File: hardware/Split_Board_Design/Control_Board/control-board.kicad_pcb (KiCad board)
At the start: 2 copper layers, 100 x 60 mm, 118 parts, among them J1 USB2.0_16P, J10 Conn_01x03, J2 UART_CONN, J3 XT30PW-M, J5 Conn_01x06, J7 Conn_01x03, J8 Conn_01x03, J9 Conn_01x02, Q2 2SD882, Q3 BC817, Q4 BC817, Q5 2SD882, Q6 2SD882, SW1 ENABLE, U1 TCAN3414DR, U10 LTV-356T, U11 LTV-356T, U12 LTV-356T, U14 LTV-356T, U15 CH340C, U2 INA240A1PW, U3 MAX3485, U4 ESP32-WROOM-32E, U5 USBLC6-2SC6, U6 LTV-356T, U7 TLV1117-33, U8 LV14340DDAR

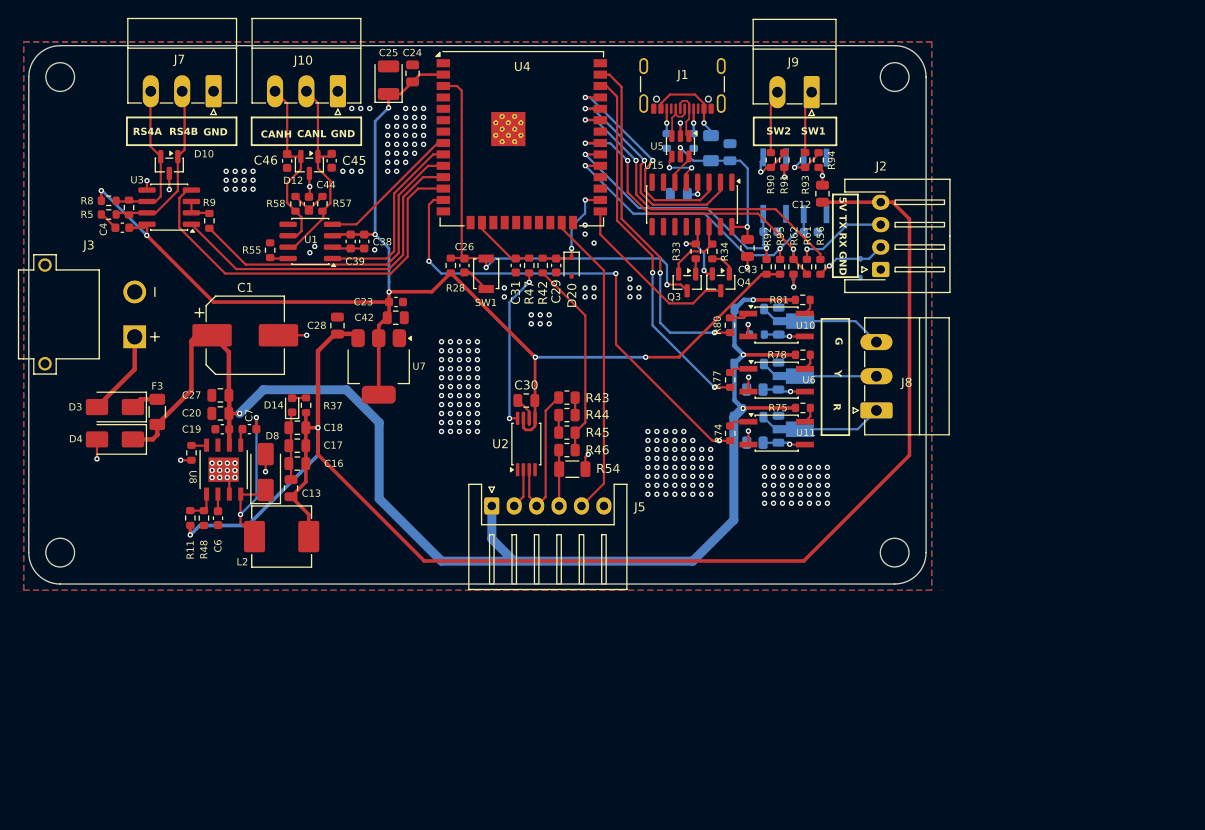
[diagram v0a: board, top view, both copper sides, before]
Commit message: feat(layout): Finished demo schematic for control board
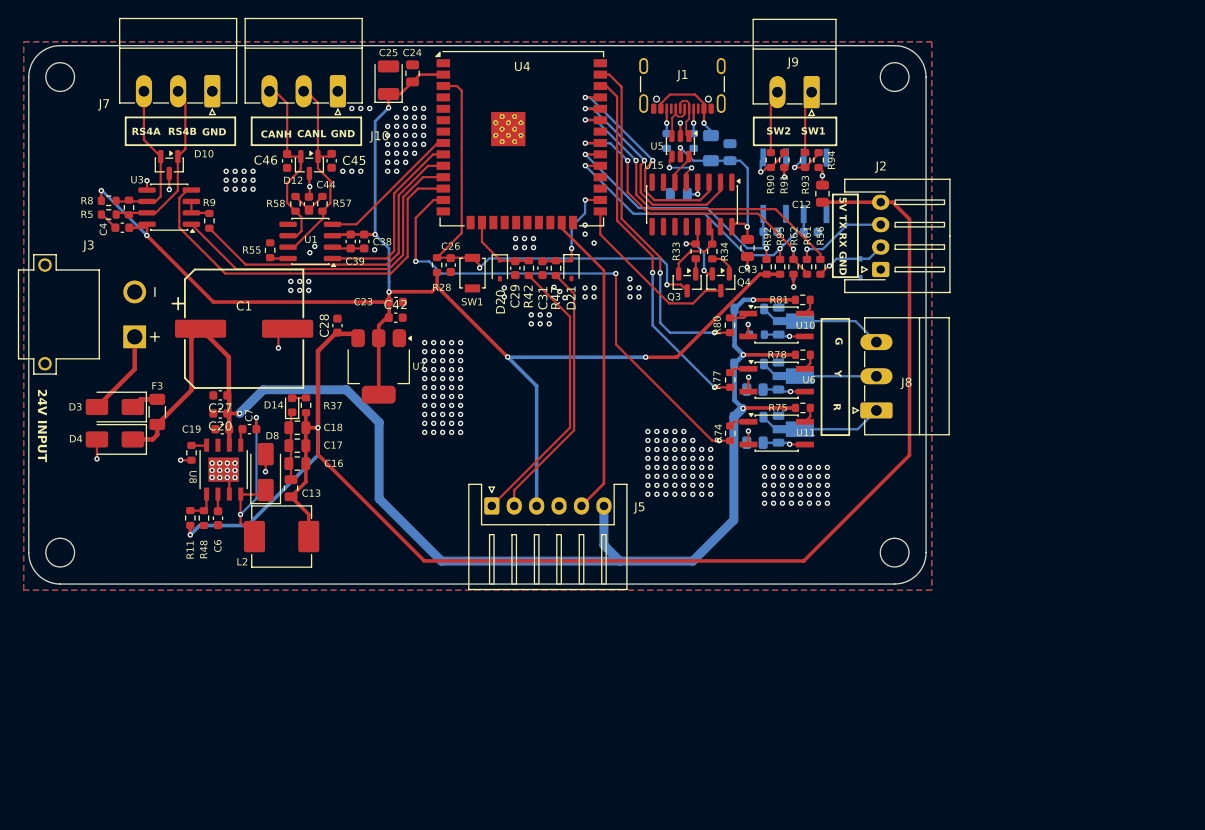
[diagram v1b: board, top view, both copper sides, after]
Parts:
- removed C30: 100nF, Capacitor_SMD:C_0805_2012Metric
- removed R43, R44, R45: 150kR, Resistor_SMD:R_0805_2012Metric
- removed R46: 18kR, Resistor_SMD:R_0805_2012Metric
- removed R54: 0R, Resistor_SMD:R_1206_3216Metric
- removed U2: INA240A1PW, Package_SO:TSSOP-8_4.4x3mm_P0.65mm
- added D21: PESD5Z3.3, Diode_SMD:D_SOD-323, F.Cu at (138.5, 62.9)
- C1: value 100uF -> 680uF-35V; footprint Capacitor_SMD:CP_Elec_8x10.5 -> RobotChargeController:CP_Elec_12.5x13.5_Generic_H13
- C20, C27, C28, C42: footprint Capacitor_SMD:C_0805_2012Metric -> Capacitor_SMD:C_0603_1608Metric
- C40, C41: value 100nF - 50V -> 100nF-50V
- J10, J7: footprint Connector_Phoenix_MC:PhoenixContact_MC_1,5_3-G-3.5_1x03_P3.50mm_Horizontal -> Connector_Phoenix_MC:PhoenixContact_MC_1,5_3-G-3.81_1x03_P3.81mm_Horizontal
- moved D20 8.01 mm to (130.5, 62.9)
- moved C29 4.56 mm to (132.2, 62.8)
- moved C31 2.99 mm to (135.2, 62.8)
- moved R47 2.99 mm to (136.8, 62.8)
- moved R42 1.58 mm to (133.7, 62.8)
- moved SW1 1.53 mm to (127.5, 63.4)
- moved R28 1.53 mm to (123.5, 62.5)
- moved C26 1.53 mm to (125.0, 62.5)
- moved C1 0.74 mm to (102.0, 69.5)
- moved J7 0.14 mm to (98.5, 43.1)
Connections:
- C29 pad 2: /MCU_Control/VOUT_SENSE_ADC -> /MCU_Control/VOUT_MCU_ADC
- C31 pad 2: /MCU_Control/IOUT_SENSE_ADC -> /MCU_Control/IOUT_MCU_ADC
- D20 pad 1: /MCU_Control/VOUT_SENSE_ADC -> /MCU_Control/VOUT_MCU_ADC
- J5 pad 1: +24V -> /MCU_Control/VOUT_SENSE_ADC
- J5 pad 2: /Output_Sensing/SHUNT_HIGH_P -> /MCU_Control/IOUT_SENSE_ADC
- J5 pad 3: /Output_Sensing/SHUNT_LOW_P -> +3V3
- J5 pad 4: 60V_GND -> GND
- J5 pad 6: GND -> +24V
- R42 pad 1: /MCU_Control/VOUT_SENSE_ADC -> /MCU_Control/VOUT_MCU_ADC
- R42 pad 2: Net-(R42-Pad2) -> /MCU_Control/VOUT_SENSE_ADC
- R47 pad 1: /MCU_Control/IOUT_SENSE_ADC -> /MCU_Control/IOUT_MCU_ADC
- R47 pad 2: Net-(R47-Pad2) -> /MCU_Control/IOUT_SENSE_ADC
- U4 pad 16: /MCU_Control/IOUT_SENSE_ADC -> /MCU_Control/VOUT_MCU_ADC
- U4 pad 26: /MCU_Control/VOUT_SENSE_ADC -> /MCU_Control/IOUT_MCU_ADC
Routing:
- net Net-(R42-Pad2): track 22.2 -> 0.00 mm
- net /MCU_Control/IOUT_SENSE_ADC: track 7.44 -> 29.3 mm
- net /MCU_Control/VOUT_SENSE_ADC: track 11.8 -> 31.2 mm, vias 2 -> 0
- net Net-(R47-Pad2): track 18.0 -> 0.00 mm, vias 2 -> 0
- net /Output_Sensing/SHUNT_LOW_P: track 17.5 -> 0.00 mm
- net /MCU_Control/IOUT_MCU_ADC: track 0.00 -> 12.1 mm, vias 0 -> 2
- net GND: track 49.4 -> 39.4 mm, vias 254 -> 268
- net +3V3: track 151.4 -> 159.7 mm
- net /MCU_Control/VOUT_MCU_ADC: track 0.00 -> 8.26 mm
- net 60V_GND: track 6.24 -> 0.00 mm
- net /Output_Sensing/SHUNT_HIGH_P: track 4.46 -> 0.00 mm
- net /MCU_Control/MCU_EN: track 51.6 -> 53.8 mm
- net /Communication_Interfaces/DO1_CMD: track 54.6 -> 56.7 mm
- net Net-(R44-Pad2): track 1.95 -> 0.00 mm
- net Net-(R43-Pad2): track 1.95 -> 0.00 mm
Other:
- board text added: "24V INPUT"

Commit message: feat(layout): Update layout
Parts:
- C12, C15, C18, C24, C43: value 100nF -> 100nF-50V; footprint Capacitor_SMD:C_0805_2012Metric -> Capacitor_SMD:C_0603_1608Metric
- C13: value 33pF -> 33pF-50V; footprint Capacitor_SMD:C_0805_2012Metric -> Capacitor_SMD:C_0603_1608Metric
- C16, C17: value 22uF -> 22uF-50V
- C21: value 10uF -> 10uF-50V; footprint Capacitor_SMD:C_0805_2012Metric -> Capacitor_SMD:C_0603_1608Metric
- C25: value 10uF -> 10uF-25V
- C6: value 22nF -> 22nF-50V
- moved F3 1.24 mm to (92.4, 80.0)
- moved C27 0.40 mm to (99.3, 77.4)
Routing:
- net +3V3: track 159.7 -> 158.8 mm
- net +24V: track 154.1 -> 154.9 mm
- net /Communication_Interfaces/DO1_CMD: vias 3 -> 2
- net GND: vias 268 -> 280
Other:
- board text added: "24V CTR GND 3V3 Vo Io"

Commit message: Some minor updates
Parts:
- C31: value 10nF-50V -> 100nF-50V
- R42: value 10kR -> 1kR
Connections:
- U4 pad 16: /MCU_Control/VOUT_MCU_ADC -> unconnected-(U4-IO13-Pad16)
- U4 pad 26: /MCU_Control/IOUT_MCU_ADC -> unconnected-(U4-IO4-Pad26)
- U4 pad 6: unconnected-(U4-IO34-Pad6) -> /MCU_Control/IOUT_MCU_ADC
- U4 pad 7: unconnected-(U4-IO35-Pad7) -> /MCU_Control/VOUT_MCU_ADC
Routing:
- net /MCU_Control/IOUT_MCU_ADC: track 12.1 -> 25.6 mm
- net /MCU_Control/VOUT_MCU_ADC: track 8.26 -> 21.0 mm, vias 0 -> 2
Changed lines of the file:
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@@
 			)
 		)
-		(property "Value" "10nF-50V"
+		(property "Value" "100nF-50V"
 			(at 0 1.43 90)
 			(layer "F.Fab")
@@
 			)
 		)
-		(property "Link to Buy" "https://linhkien.cxtvn.com/2353-tu-103-10nf-0603-50v-10-20c.html"
+		(property "Link to Buy" "https://linhkien.cxtvn.com/1981-tu-0603-khong-phan-cuc.html"
 			(at 0 0 90)
 			(unlocked yes)
@@
 			)
 		)
-		(property "Value" "10kR"
+		(property "Value" "1kR"
 			(at 0 1.43 90)
 			(layer "F.Fab")
@@
 			(size 1.5 0.9)
 			(layers "F.Cu" "F.Mask" "F.Paste")
-			(net "unconnected-(U4-IO34-Pad6)")
+			(net "/MCU_Control/IOUT_MCU_ADC")
 			(pinfunction "IO34_6")
-			(pintype "input+no_connect")
+			(pintype "input")
 		)
 		(pad "7" smd rect
@@
 			(size 1.5 0.9)
 			(layers "F.Cu" "F.Mask" "F.Paste")
-			(net "unconnected-(U4-IO35-Pad7)")
+			(net "/MCU_Control/VOUT_MCU_ADC")
 			(pinfunction "IO35_7")
-			(pintype "input+no_connect")
+			(pintype "input")
 		)
 		(pad "8" smd rect
@@
 			(size 1.5 0.9)
 			(layers "F.Cu" "F.Mask" "F.Paste")
-			(net "/MCU_Control/VOUT_MCU_ADC")
+			(net "unconnected-(U4-IO13-Pad16)")
 			(pinfunction "IO13_16")
-			(pintype "bidirectional")
+			(pintype "bidirectional+no_connect")
 		)
 		(pad "17" smd rect
@@
 			(size 1.5 0.9)
 			(layers "F.Cu" "F.Mask" "F.Paste")
-			(net "/MCU_Control/IOUT_MCU_ADC")
+			(net "unconnected-(U4-IO4-Pad26)")
 			(pinfunction "IO4_26")
-			(pintype "bidirectional")
+			(pintype "bidirectional+no_connect")
 		)
 		(pad "27" smd rect
@@
 	)
 	(segment
-		(start 126.25 43.025)
-		(end 125.725 42.5)
+		(start 123.505 61.625)
+		(end 126.35 58.78)
 		(width 0.25)
 		(layer "F.Cu")
@@
 	)
 	(segment
-		(start 125.725 42.5)
-		(end 124.2 42.5)
+		(start 126.35 58.78)
+		(end 126.35 43.125)
 		(width 0.25)
 		(layer "F.Cu")
@@
 	)
 	(segment
-		(start 123.505 61.625)
-		(end 126.25 58.88)
+		(start 127.45 61.65)
+		(end 128.25 62.45)
 		(width 0.25)
 		(layer "F.Cu")
@@
 	)
 	(segment
-		(start 127.45 61.65)
-		(end 128.25 62.45)
+		(start 125.725 42.5)
+		(end 124.2 42.5)
 		(width 0.25)
 		(layer "F.Cu")
@@
 	)
 	(segment
-		(start 126.25 58.88)
-		(end 126.25 43.025)
+		(start 126.35 43.125)
+		(end 125.725 42.5)
 		(width 0.25)
 		(layer "F.Cu")
@@
 	)
 	(segment
+		(start 125.535 46.31)
+		(end 125.55 46.325)
+		(width 0.25)
+		(layer "F.Cu")
+		(net "/MCU_Control/IOUT_MCU_ADC")
+	)
+	(segment
 		(start 138.5 60.6)
 		(end 138.5 61.825)
@@
 	)
 	(segment
-		(start 141.7 55.2)
-		(end 140.225 55.2)
+		(start 124.2 46.31)
+		(end 125.535 46.31)
 		(width 0.25)
 		(layer "F.Cu")
@@
 	)
 	(via
-		(at 140.025 55.2)
+		(at 138.5 60.6)
 		(size 0.6)
 		(drill 0.3)
@@
 	)
 	(via
-		(at 138.5 60.6)
+		(at 125.55 46.325)
 		(size 0.6)
 		(drill 0.3)
@@
 	)
 	(segment
-		(start 140 56.675)
-		(end 140 55.225)
+		(start 138.5 60.6)
+		(end 138.5 59.275)
 		(width 0.25)
 		(layer "B.Cu")
@@
 	)
 	(segment
-		(start 140 55.225)
-		(end 140.025 55.2)
+		(start 138.5 59.275)
+		(end 125.55 46.325)
 		(width 0.25)
 		(layer "B.Cu")
@@
 	)
 	(segment
-		(start 138.5 60.6)
-		(end 138.5 58.175)
+		(start 124.2 47.58)
+		(end 125.58 47.58)
 		(width 0.25)
-		(layer "B.Cu")
-		(net "/MCU_Control/IOUT_MCU_ADC")
+		(layer "F.Cu")
+		(net "/MCU_Control/VOUT_MCU_ADC")
 	)
 	(segment
-		(start 138.5 58.175)
-		(end 140 56.675)
+		(start 125.58 47.58)
+		(end 125.6 47.6)
 		(width 0.25)
-		(layer "B.Cu")
-		(net "/MCU_Control/IOUT_MCU_ADC")
+		(layer "F.Cu")
+		(net "/MCU_Control/VOUT_MCU_ADC")
 	)
 	(segment
-		(start 130.5 61.875)
-		(end 128.505 59.88)
+		(start 130.5 60.8)
+		(end 130.5 61.875)
 		(width 0.25)
 		(layer "F.Cu")
@@
 	)
 	(segment
-		(start 128.505 59.88)
-		(end 128.505 57.72)
+		(start 130.625 61.97)
+		(end 130.5 61.845)
 		(width 0.25)
 		(layer "F.Cu")
@@
 	)
 	(segment
-		(start 130.625 61.97)
-		(end 130.5 61.845)
+		(start 130.525 60.775)
+		(end 130.5 60.8)
 		(width 0.25)
 		(layer "F.Cu")
@@
 		(net "/MCU_Control/VOUT_MCU_ADC")
 	)
+	(via
+		(at 125.6 47.6)
+		(size 0.6)
+		(drill 0.3)
+		(layers "F.Cu" "B.Cu")
+		(net "/MCU_Control/VOUT_MCU_ADC")
+	)
+	(via
+		(at 130.525 60.775)
+		(size 0.6)
+		(drill 0.3)
+		(layers "F.Cu" "B.Cu")
+		(net "/MCU_Control/VOUT_MCU_ADC")
+	)
+	(segment
+		(start 128.505 50.505)
+		(end 125.6 47.6)
+		(width 0.25)
+		(layer "B.Cu")
+		(net "/MCU_Control/VOUT_MCU_ADC")
+	)
+	(segment
+		(start 130.525 60.775)
+		(end 128.505 58.755)
+		(width 0.25)
+		(layer "B.Cu")
+		(net "/MCU_Control/VOUT_MCU_ADC")
+	)
+	(segment
+		(start 128.505 58.755)
+		(end 128.505 50.505)
+		(width 0.25)
+		(layer "B.Cu")
+		(net "/MCU_Control/VOUT_MCU_ADC")
+	)

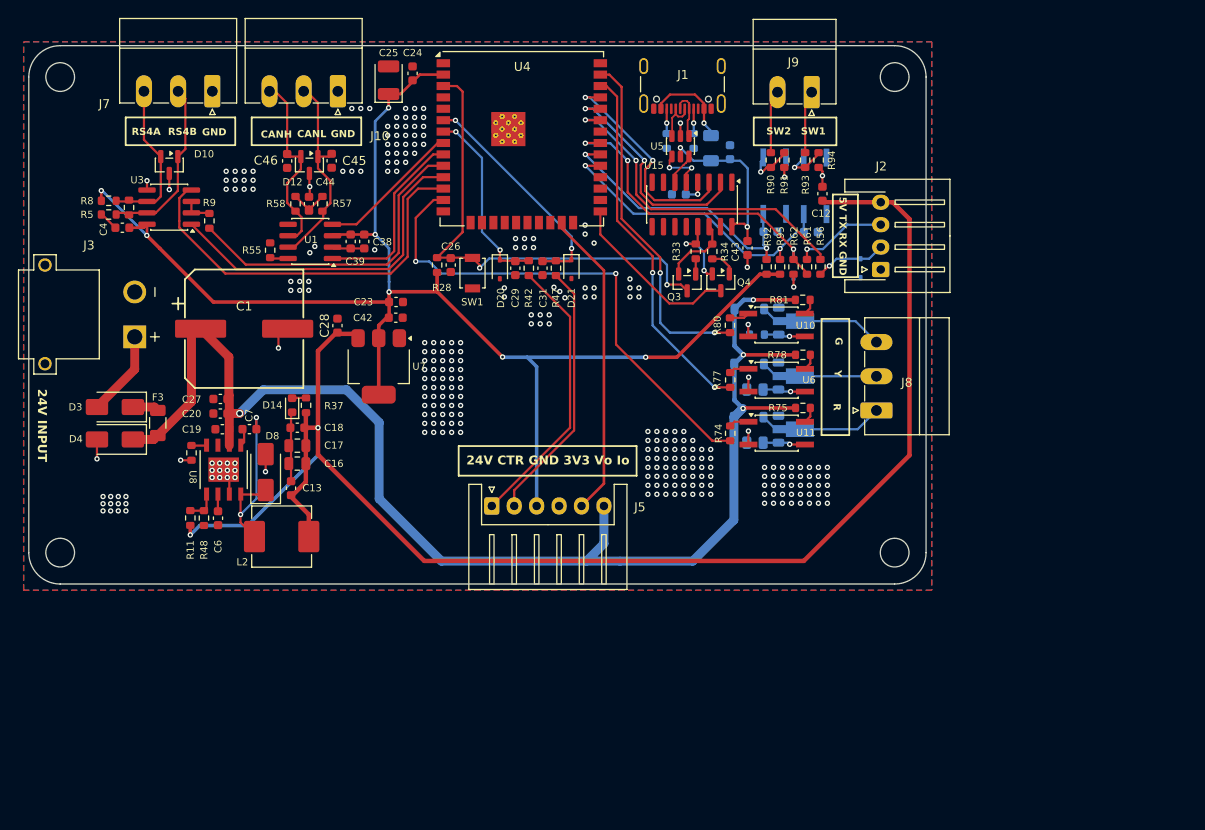
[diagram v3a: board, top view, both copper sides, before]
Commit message: feat(layout): update control board layout
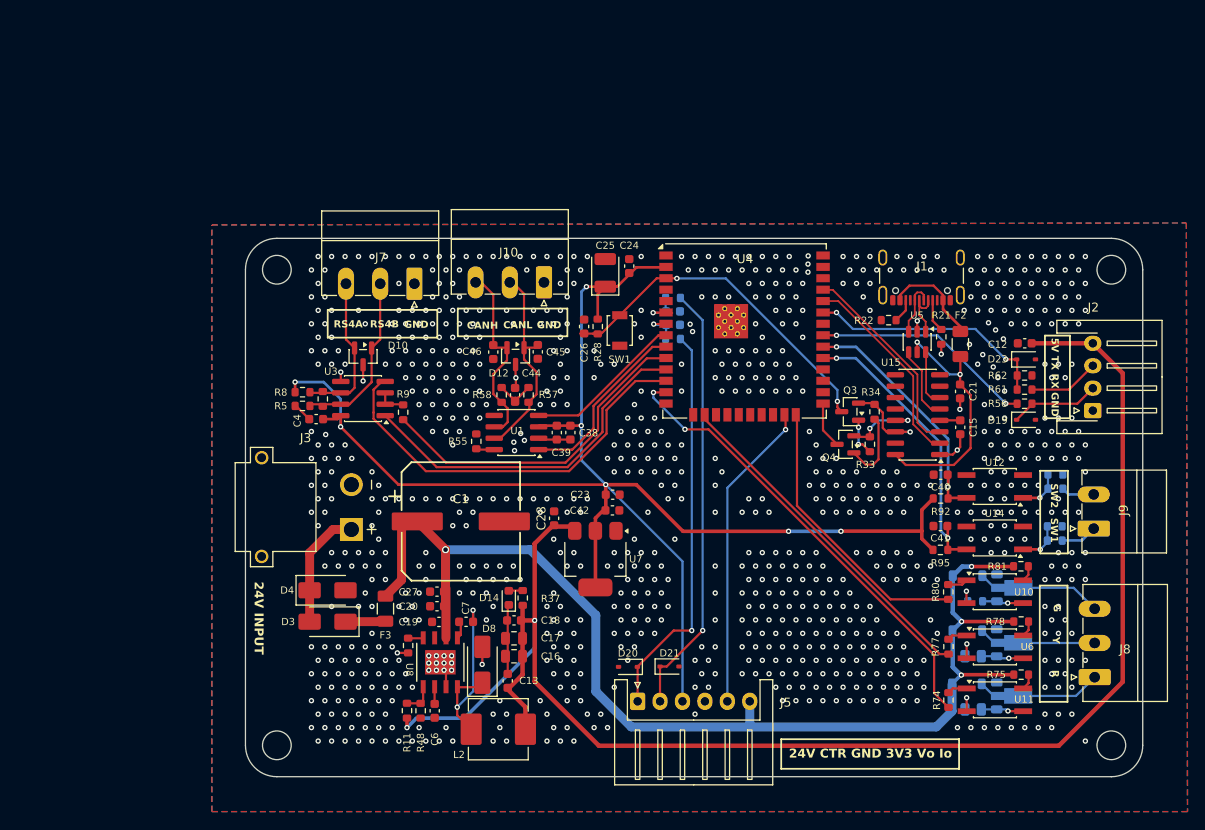
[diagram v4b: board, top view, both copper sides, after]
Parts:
- removed C43: 100nF-50V, Capacitor_SMD:C_0603_1608Metric
- C15, C21, C40, C41, D19, D23, F2, R21, R22, U12, U14: moved to F.Cu
- C29, C31, R42, R47, R90, R91, R93, R94: moved to B.Cu
- moved J9 57.9 mm to (196.7, 91.8), turned to 90 degrees
- moved R93 50.7 mm to (192.3, 93.2), turned to 180 degrees
- moved R94 48.6 mm to (192.3, 91.6), turned to 0 degrees
- moved R90 48.4 mm to (192.4, 87.4), turned to 180 degrees
- moved D20 46.6 mm to (144.8, 107.2), turned to 180 degrees
- moved R91 46.3 mm to (192.4, 85.8), turned to 0 degrees
- moved D21 45.6 mm to (149.4, 107.2), turned to 0 degrees
- moved U14 44.1 mm to (185.7, 92.9), turned to 180 degrees
- moved U12 41.5 mm to (185.7, 87.1), turned to 180 degrees
- moved C15 40.7 mm to (181.8, 80.5), turned to -90 degrees
- moved D1 38.4 mm to (182.5, 109.1)
- moved U11 38.4 mm to (185.7, 110.9)
- moved U6 38.4 mm to (185.7, 105.0)
- moved D5 38.4 mm to (182.6, 103.2)
- moved D6 38.4 mm to (182.6, 97.1)
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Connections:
- D20 pad 1: /MCU_Control/VOUT_MCU_ADC -> /MCU_Control/VOUT_SENSE_ADC
- D21 pad 1: /MCU_Control/IOUT_MCU_ADC -> /MCU_Control/IOUT_SENSE_ADC
- D4 pad 1: +24V -> /Auxiliary_Power_Supply/VAUX_IN_P
- U4 pad 16: unconnected-(U4-IO13-Pad16) -> /Communication_Interfaces/DO2_CMD
- U4 pad 24: unconnected-(U4-IO2-Pad24) -> /Communication_Interfaces/DO3_CMD
- U4 pad 31: /Communication_Interfaces/UART_EXT_RX_MCU -> /Communication_Interfaces/UART_EXT_TX_MCU
- U4 pad 33: /Communication_Interfaces/UART_EXT_TX_MCU -> /Communication_Interfaces/UART_EXT_RX_MCU
- U4 pad 36: /Communication_Interfaces/DO2_CMD -> unconnected-(U4-IO22-Pad36)
- U4 pad 37: /Communication_Interfaces/DO3_CMD -> unconnected-(U4-IO23-Pad37)
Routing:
- net /MCU_Control/IOUT_MCU_ADC: track 25.6 -> 4.64 mm, vias 2 -> 1
- net /MCU_Control/IOUT_SENSE_ADC: track 29.3 -> 48.4 mm, vias 0 -> 1
- net /MCU_Control/VOUT_MCU_ADC: track 21.0 -> 4.73 mm, vias 2 -> 1
- net /MCU_Control/MCU_EN: track 53.9 -> 39.0 mm
- net /MCU_Control/MCU_BOOT: track 19.8 -> 5.30 mm
- net +24V: track 154.9 -> 141.3 mm
- net /MCU_Control/VOUT_SENSE_ADC: track 31.2 -> 44.7 mm, vias 0 -> 1
- net +3V3: track 158.8 -> 171.3 mm
- net /Communication_Interfaces/UART_EXT_TX_MCU: track 37.0 -> 24.7 mm
- net /Communication_Interfaces/UART_EXT_RX_MCU: track 36.2 -> 27.0 mm, vias 3 -> 2
- net +5V: track 168.2 -> 176.6 mm
- net /Communication_Interfaces/DO3_CMD: track 39.2 -> 31.3 mm, vias 2 -> 0
- net V_USB: track 19.5 -> 27.4 mm
- net Net-(Q4-B): track 3.08 -> 8.18 mm
- net /Communication_Interfaces/DO1_CMD: track 56.7 -> 51.8 mm
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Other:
- board text added: "{ "ViaStitching": "0.3.0", "stitch_zone_0": { "HSpacing": "1.5", "VSpacing": "1.5", "HOffset": "0", "VOffset": "0", "Clearance": "0", "Randomize": false, "Stagger": true, "OnlyFilledCopper": true } }"
- board text added: "{ "ViaStitching": "0.3.0", "stitch_zone_0": { "HSpacing": "3", "VSpacing": "3", "HOffset": "0", "VOffset": "0", "Clearance": "0.5", "Randomize": false, "Stagger": true, "OnlyFilledCopper": true } }"
